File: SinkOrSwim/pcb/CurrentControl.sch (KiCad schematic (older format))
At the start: 8 parts, among them P201 CONN_01X01, Q201 BUK9575-100A, U201 LMV358

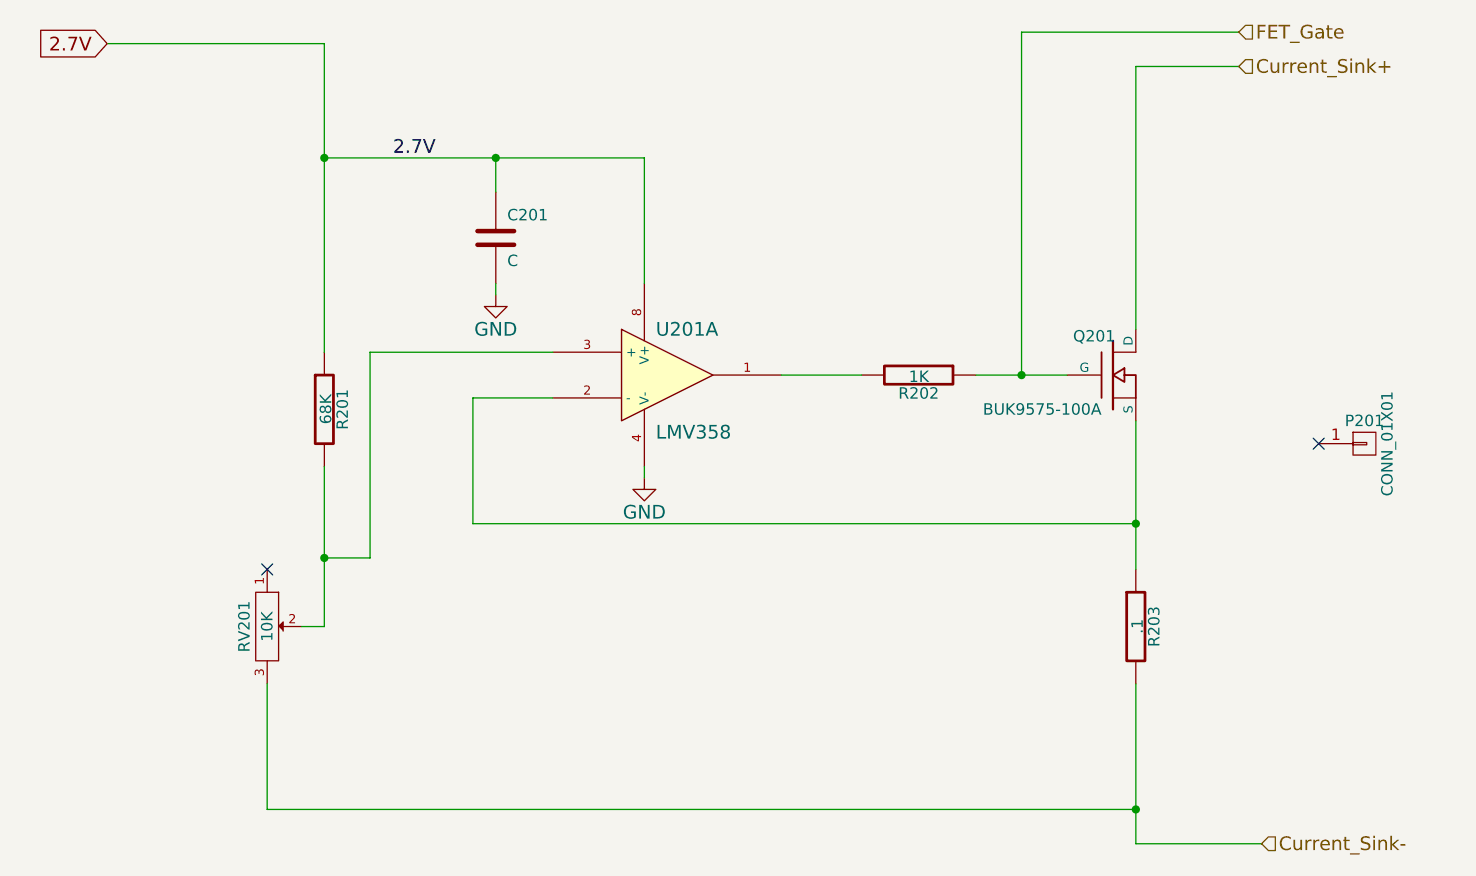
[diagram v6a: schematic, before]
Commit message: Better Layout.  Added 2 1x2 pin headers to be able to test current.
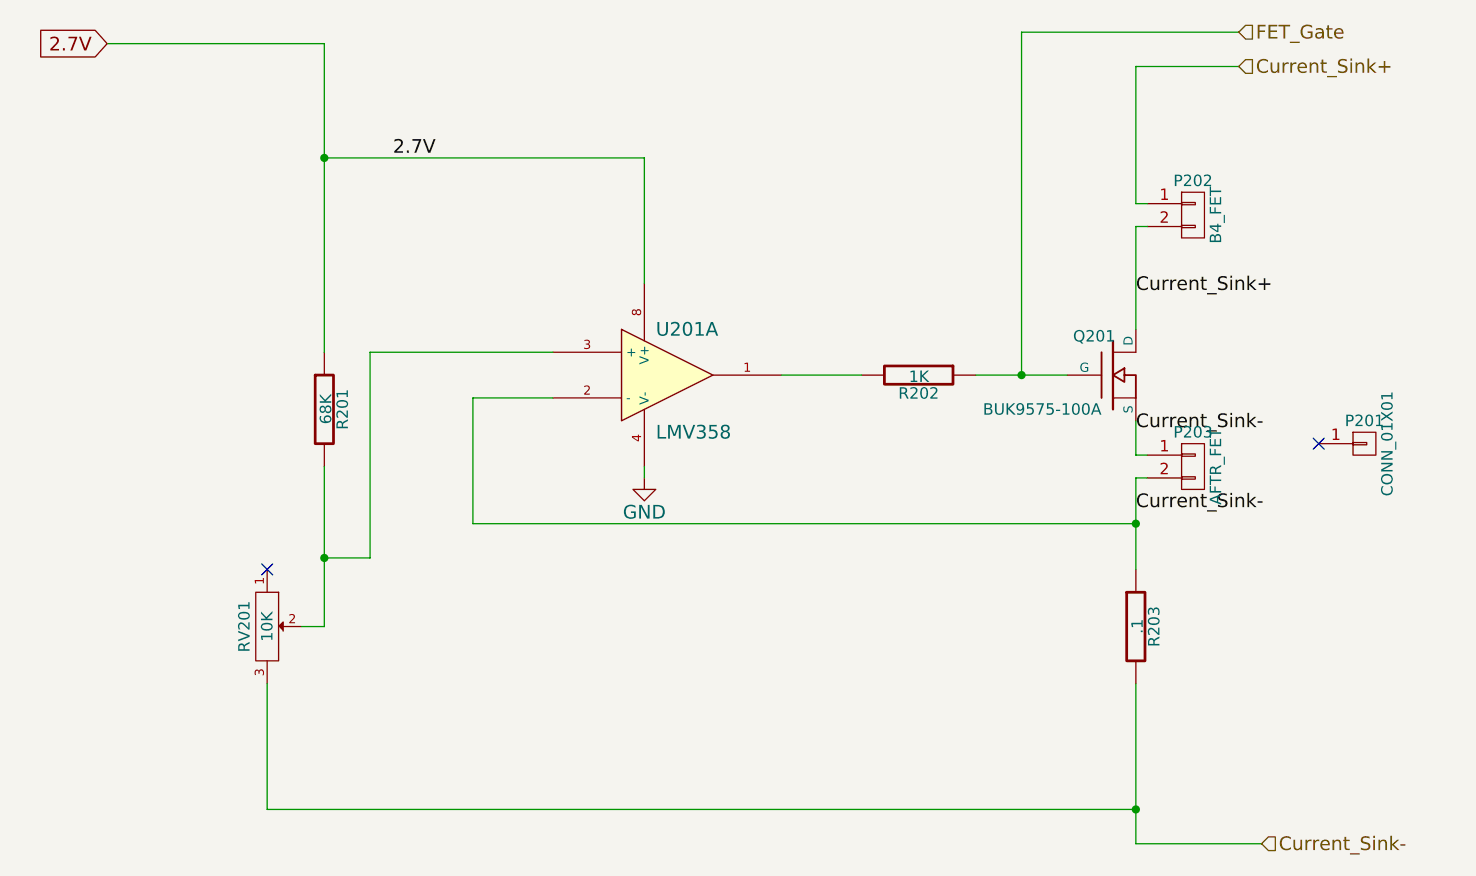
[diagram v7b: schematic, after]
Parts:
- removed C201: C, Capacitors_SMD:C_0805_HandSoldering, symbol C
- added P202: B4_FET, Pin_Headers:Pin_Header_Straight_1x02, symbol CONN_01X02
- added P203: AFTR_FET, Pin_Headers:Pin_Header_Straight_1x02, symbol CONN_01X02
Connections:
- net Current_Sink+: now also P202.1 (P1), P202.2 (P2)
- net Current_Sink-: now also Q201.S, R203.1, U201.2 (-), P203.1 (P1), P203.2 (P2)
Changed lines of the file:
@@
 	1    0    0    -1
 $EndComp
-Wire Wire Line
-	7900 3300 7900 3950
-Wire Wire Line
-	7900 4450 7900 5150
 $Comp
 L GND #PWR03
@@
 	1    0    0    -1
 $EndComp
-Wire Wire Line
-	5750 3550 5750 3500
-Wire Wire Line
-	5350 3200 5000 3200
-Wire Wire Line
-	5000 3200 5000 3750
-Wire Wire Line
-	5000 3750 7900 3750
-Connection ~ 7900 3750
-Wire Wire Line
-	4550 3900 4550 3000
-Wire Wire Line
-	4550 3000 5350 3000
-Wire Wire Line
-	4100 4450 4100 5000
-Wire Wire Line
-	4100 5000 7900 5000
-Connection ~ 7900 5000
-Wire Wire Line
-	4350 2150 5750 2150
-Connection ~ 4350 2150
 Text Label 4650 2150 0    60   ~ 0
 2.7V
-Wire Wire Line
-	7900 1750 7900 2900
-$Comp
-L C C201
-U 1 1 54DC4901
-P 5100 2500
-F 0 "C201" H 5150 2600 50  0000 L CNN
-F 1 "C" H 5150 2400 50  0000 L CNN
-F 2 "Capacitors_SMD:C_0805_HandSoldering" H 5138 2350 30  0001 C CNN
-F 3 "" H 5100 2500 60  0000 C CNN
-	1    5100 2500
-	1    0    0    -1
-$EndComp
-Wire Wire Line
-	5100 2300 5100 2150
-Connection ~ 5100 2150
-$Comp
-L GND #PWR04
-U 1 1 54DC490A
-P 5100 2750
-F 0 "#PWR04" H 5100 2500 60  0001 C CNN
-F 1 "GND" H 5100 2600 60  0000 C CNN
-F 2 "" H 5100 2750 60  0000 C CNN
-F 3 "" H 5100 2750 60  0000 C CNN
-	1    5100 2750
-	1    0    0    -1
-$EndComp
-Wire Wire Line
-	5100 2750 5100 2700
 $Comp
 L LMV358 U201
@@
 Text GLabel 3400 1650 0    60   Input ~ 0
 2.7V
-Wire Wire Line
-	3400 1650 4350 1650
-Wire Wire Line
-	4350 1650 4350 3000
 Text HLabel 8350 1750 2    60   Input ~ 0
 Current_Sink+
-Wire Wire Line
-	7900 1750 8350 1750
 $Comp
 L R R202
@@
 	0    1    1    0
 $EndComp
-Wire Wire Line
-	6350 3100 6700 3100
-Wire Wire Line
-	7200 3100 7600 3100
-Wire Wire Line
-	7400 3100 7400 1600
-Wire Wire Line
-	7400 1600 8350 1600
-Connection ~ 7400 3100
 Text HLabel 8350 1600 2    60   Input ~ 0
 FET_Gate
-Wire Wire Line
-	7900 5150 8450 5150
 Text HLabel 8450 5150 2    60   Input ~ 0
 Current_Sink-
@@
 $EndComp
 NoConn ~ 8700 3400
-Connection ~ 4350 3900
-Wire Wire Line
-	4350 3900 4550 3900
 $Comp
 L POT RV201
@@
 	0    1    1    0
 $EndComp
+NoConn ~ 4100 3950
+$Comp
+L CONN_01X02 P202
+U 1 1 54E8A789
+P 8150 2400
+F 0 "P202" H 8150 2550 50  0000 C CNN
+F 1 "B4_FET" V 8250 2400 50  0000 C CNN
+F 2 "Pin_Headers:Pin_Header_Straight_1x02" H 8150 2400 60  0001 C CNN
+F 3 "" H 8150 2400 60  0000 C CNN
+	1    8150 2400
+	1    0    0    -1
+$EndComp
+$Comp
+L CONN_01X02 P203
+U 1 1 54E8A830
+P 8150 3500
+F 0 "P203" H 8150 3650 50  0000 C CNN
+F 1 "AFTR_FET" V 8250 3500 50  0000 C CNN
+F 2 "Pin_Headers:Pin_Header_Straight_1x02" H 8150 3500 60  0001 C CNN
+F 3 "" H 8150 3500 60  0000 C CNN
+	1    8150 3500
+	1    0    0    -1
+$EndComp
+Wire Wire Line
+	7900 3550 7900 3950
+Wire Wire Line
+	7950 3550 7900 3550
+Wire Wire Line
+	7900 3450 7950 3450
+Wire Wire Line
+	7900 3300 7900 3450
+Wire Wire Line
+	7900 2450 7900 2900
+Wire Wire Line
+	7950 2450 7900 2450
+Wire Wire Line
+	7900 2350 7950 2350
+Wire Wire Line
+	7900 1750 7900 2350
+Wire Wire Line
+	5750 2150 5750 2700
+Wire Wire Line
+	4350 3500 4350 4200
 Wire Wire Line
 	4350 4200 4250 4200
 Wire Wire Line
-	4350 3500 4350 4200
+	4350 3900 4550 3900
+Connection ~ 4350 3900
 Wire Wire Line
-	5750 2150 5750 2700
-NoConn ~ 4100 3950
+	7900 5150 8450 5150
+Connection ~ 7400 3100
+Wire Wire Line
+	7400 1600 8350 1600
+Wire Wire Line
+	7400 3100 7400 1600
+Wire Wire Line
+	7200 3100 7600 3100
+Wire Wire Line
+	6350 3100 6700 3100
+Wire Wire Line
+	7900 1750 8350 1750
+Wire Wire Line
+	4350 1650 4350 3000
+Wire Wire Line
+	3400 1650 4350 1650
+Connection ~ 4350 2150
+Wire Wire Line
+	4350 2150 5750 2150
+Connection ~ 7900 5000
+Wire Wire Line
+	4100 5000 7900 5000
+Wire Wire Line
+	4100 4450 4100 5000
+Wire Wire Line
+	4550 3000 5350 3000
+Wire Wire Line
+	4550 3900 4550 3000
+Connection ~ 7900 3750
+Wire Wire Line
+	5000 3750 7900 3750
+Wire Wire Line
+	5000 3200 5000 3750
+Wire Wire Line
+	5350 3200 5000 3200
+Wire Wire Line
+	5750 3550 5750 3500
+Wire Wire Line
+	7900 4450 7900 5150
+Text Label 7900 2750 0    60   ~ 0
+Current_Sink+
+Text Label 7900 3350 0    60   ~ 0
+Current_Sink-
+Text Label 7900 3700 0    60   ~ 0
+Current_Sink-
 $EndSCHEMATC

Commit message: Gerbers added, BOM written
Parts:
- P201: value CONN_01X01 -> HEATSINK; MPN (none) -> FA-T220-38E
- Q201: MPN (none) -> \"BUK9575-100A,127\"
- R201: MPN Value -> RMCF0805FT68K0
- R202: MPN (none) -> RMCF0805FT1K00
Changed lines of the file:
@@
 F 1 "68K" V 4357 3251 50  0000 C CNN
 F 2 "Resistors_SMD:R_0805_HandSoldering" V 4280 3250 30  0001 C CNN
-F 3 "" H 4350 3250 30  0000 C CNN
-F 4 "Value" H 4350 3250 60  0001 C CNN "MPN"
+F 3 "http://www.seielect.com/Catalog/SEI-RMCF_RMCP.pdf" H 4350 3250 30  0001 C CNN
+F 4 "RMCF0805FT68K0" H 4350 3250 60  0001 C CNN "MPN"
 	1    4350 3250
 	1    0    0    -1
@@
 F 1 "BUK9575-100A" H 7750 2950 50  0000 R CNN
 F 2 "Transistors_TO-220:TO-220_FET-GDS_Vertical" H 7800 3100 60  0001 C CNN
-F 3 "" H 7800 3100 60  0000 C CNN
+F 3 "http://www.nxp.com/documents/data_sheet/BUK9575_9675-100A.pdf" H 7800 3100 60  0001 C CNN
+F 4 "\"BUK9575-100A,127\"" H 7800 3100 60  0001 C CNN "MPN"
 	1    7800 3100
 	1    0    0    -1
@@
 F 1 "1K" V 6957 3101 50  0000 C CNN
 F 2 "Resistors_SMD:R_0805_HandSoldering" V 6880 3100 30  0001 C CNN
-F 3 "" H 6950 3100 30  0000 C CNN
+F 3 "http://www.seielect.com/Catalog/SEI-RMCF_RMCP.pdf" H 6950 3100 30  0001 C CNN
+F 4 "RMCF0805FT1K00" H 6950 3100 60  0001 C CNN "MPN"
 	1    6950 3100
 	0    1    1    0
@@
 P 8900 3400
 F 0 "P201" H 8900 3500 50  0000 C CNN
-F 1 "CONN_01X01" V 9000 3400 50  0000 C CNN
+F 1 "HEATSINK" V 9000 3400 50  0000 C CNN
 F 2 "pcb:FA-T220-38E" H 8900 3400 60  0001 C CNN
-F 3 "" H 8900 3400 60  0000 C CNN
+F 3 "http://media.digikey.com/pdf/Data%20Sheets/Ohmite%20PDFs/F_R_Series.pdf" H 8900 3400 60  0001 C CNN
+F 4 "FA-T220-38E" H 8900 3400 60  0001 C CNN "MPN"
 	1    8900 3400
 	1    0    0    -1
